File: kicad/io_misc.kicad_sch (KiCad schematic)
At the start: 43 parts, among them U11 microSD

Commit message: Pick JLCPCB parts for the whole BOM and add BOM/CPL generation
Adds bom/parts.csv (LCSC numbers and MPNs), scripts to apply it to the schematic and
board and to generate the JLCPCB BOM, CPL and a live stock report. Swaps the
BOOTSEL/RESET switch to a basic 5.1 mm part with a matching footprint, and replaces
out-of-stock parts (SS54, WS2812B, 10u caps, SWD header).

Co-Authored-By: Claude Sonnet 5.5 <noreply@anthropic.com>
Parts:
- C50, C52: LCSC (none) -> C307331; MPN (none) -> CL05B104KB54PNC
- C51: LCSC (none) -> C15850; MPN (none) -> CL21A106KAYNNNE
- D42: LCSC C2846931 -> C2874885; MPN WS2812B-V5 -> WS2812B-V5/W
- R102, R103, R104, R105, R106, R107: LCSC (none) -> C25744; MPN (none) -> 0402WGF1002TCE
- R108: LCSC (none) -> C25076; MPN (none) -> 0402WGF1000TCE
- R109, R110: LCSC (none) -> C25117; MPN (none) -> 0402WGF4700TCE
- R111, R112: LCSC (none) -> C25900; MPN (none) -> 0402WGF4701TCE

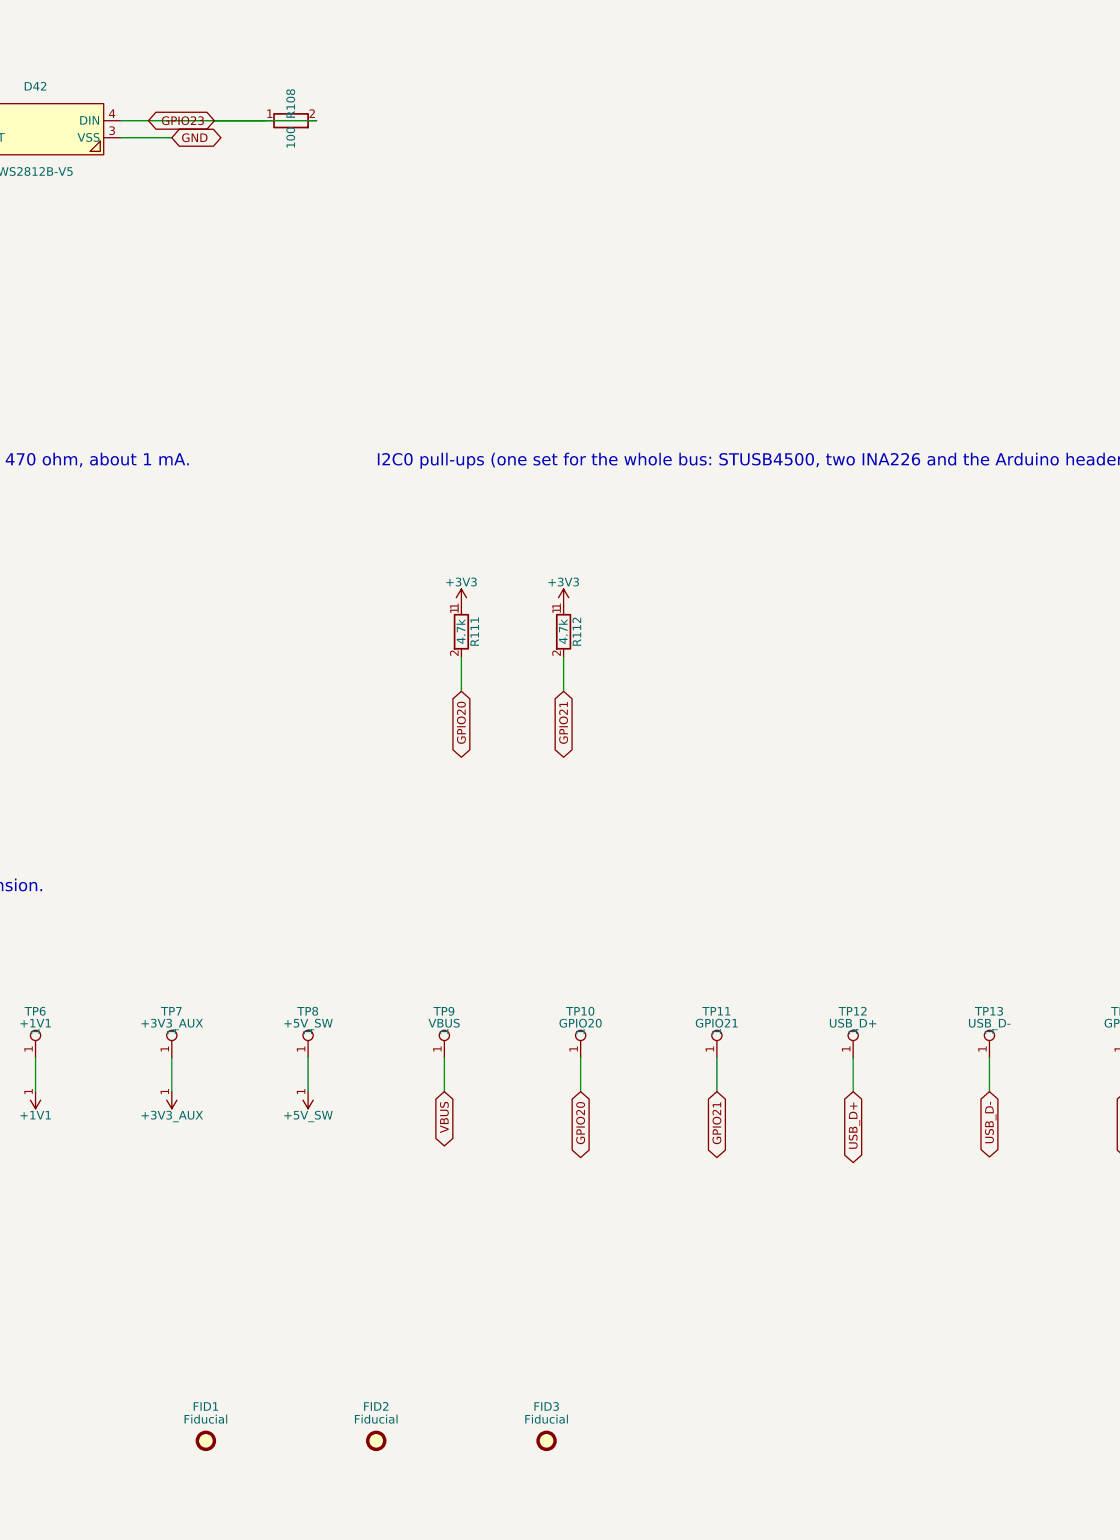
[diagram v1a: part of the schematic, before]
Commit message: Rework board layout, swap SWD header to through-hole, add Qwiic port
- SWD (J10) is now a 1x3 2.54 mm through-hole pin header footprint
  (SWCLK, GND, SWDIO) instead of the JST SH connector; removed from the
  JLCPCB BOM.
- Add J20 Qwiic connector (XY-SM04B-SRSS-TB) on the I2C bus: GND, +3V3,
  GPIO20 (SDA), GPIO21 (SCL), mounting tabs to GND.
- Placement/routing progress and the helper scripts used for it.

DRC still reports open items (unrouted RUN/GPIO24/GPIO29/QSPI_SD0 nets,
R108/GPIO23 and NT1/GPIO20 shorts, J12 edge clearance, silkscreen
overlaps); to be fixed in follow-up commits.

Co-Authored-By: Claude Sonnet 5.5 <noreply@anthropic.com>
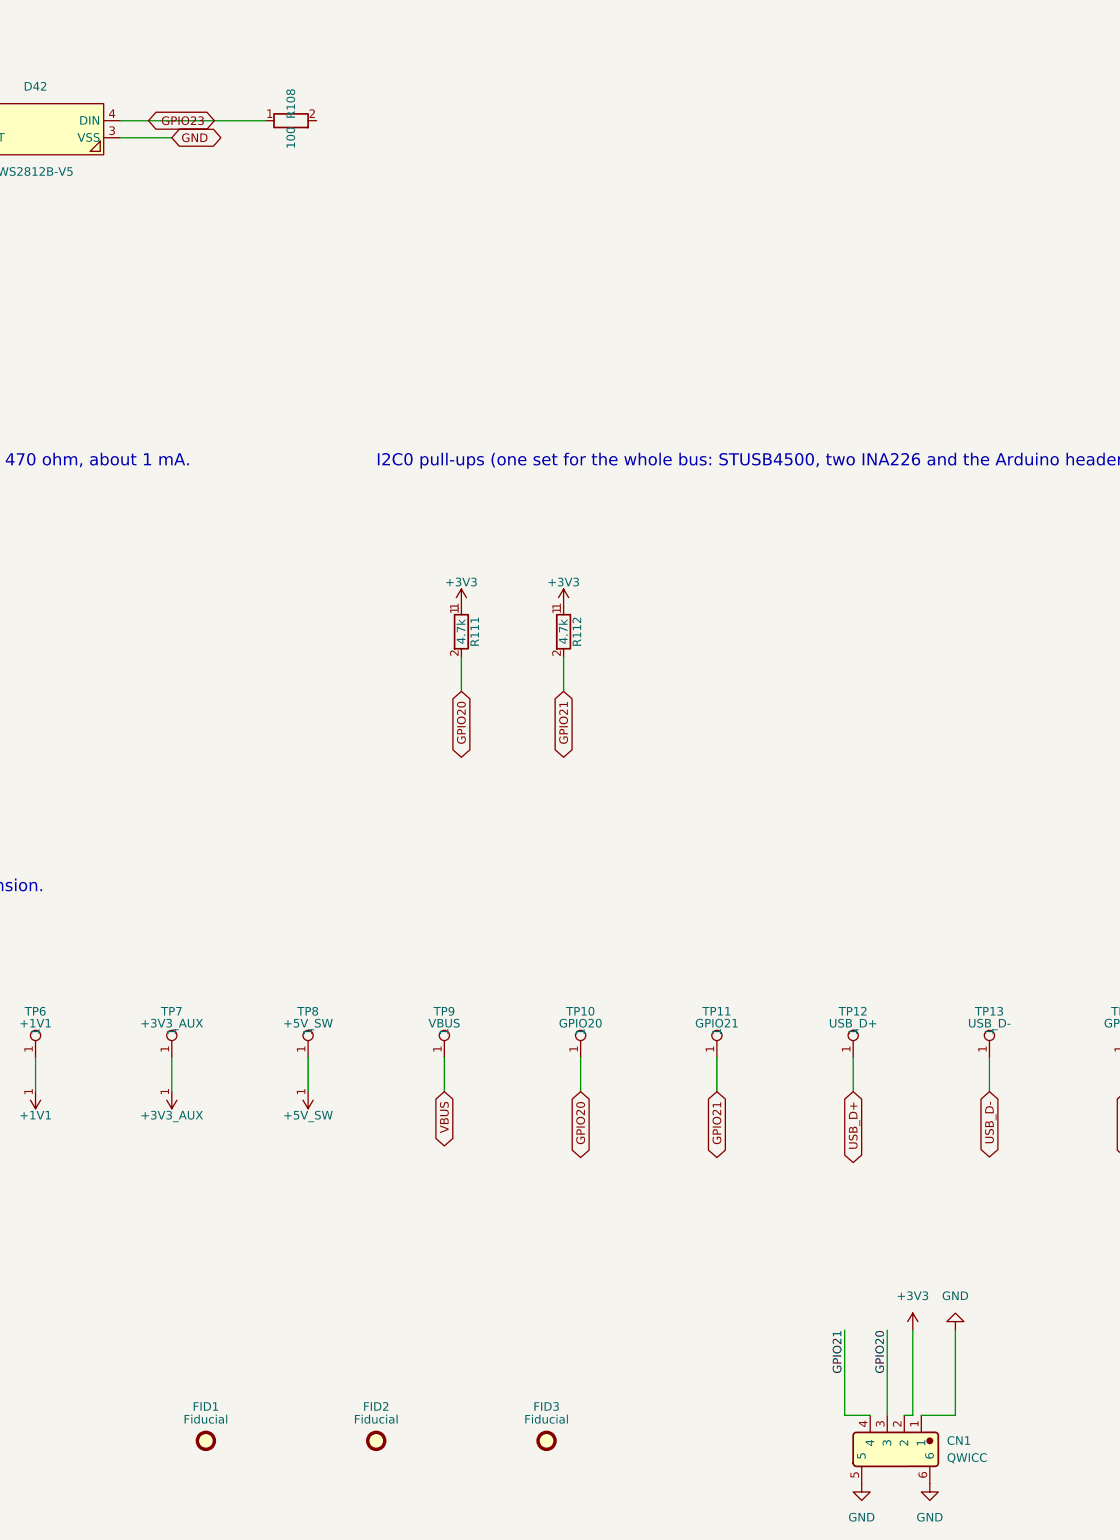
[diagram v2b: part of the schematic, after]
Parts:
- added CN1: QWICC, JLCImport:XY-SM04B-SRSS-TB, symbol JLCImport:XY-SM04B-SRSS-TB
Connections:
- net +3V3: now also CN1.2
- net GND: now also CN1.1, CN1.5, CN1.6
- net GPIO20: now also CN1.3
- net GPIO21: now also CN1.4
- net GPIO23: no longer R108.2
